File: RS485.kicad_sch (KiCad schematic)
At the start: 11 parts, among them U12 ADM1491EBR

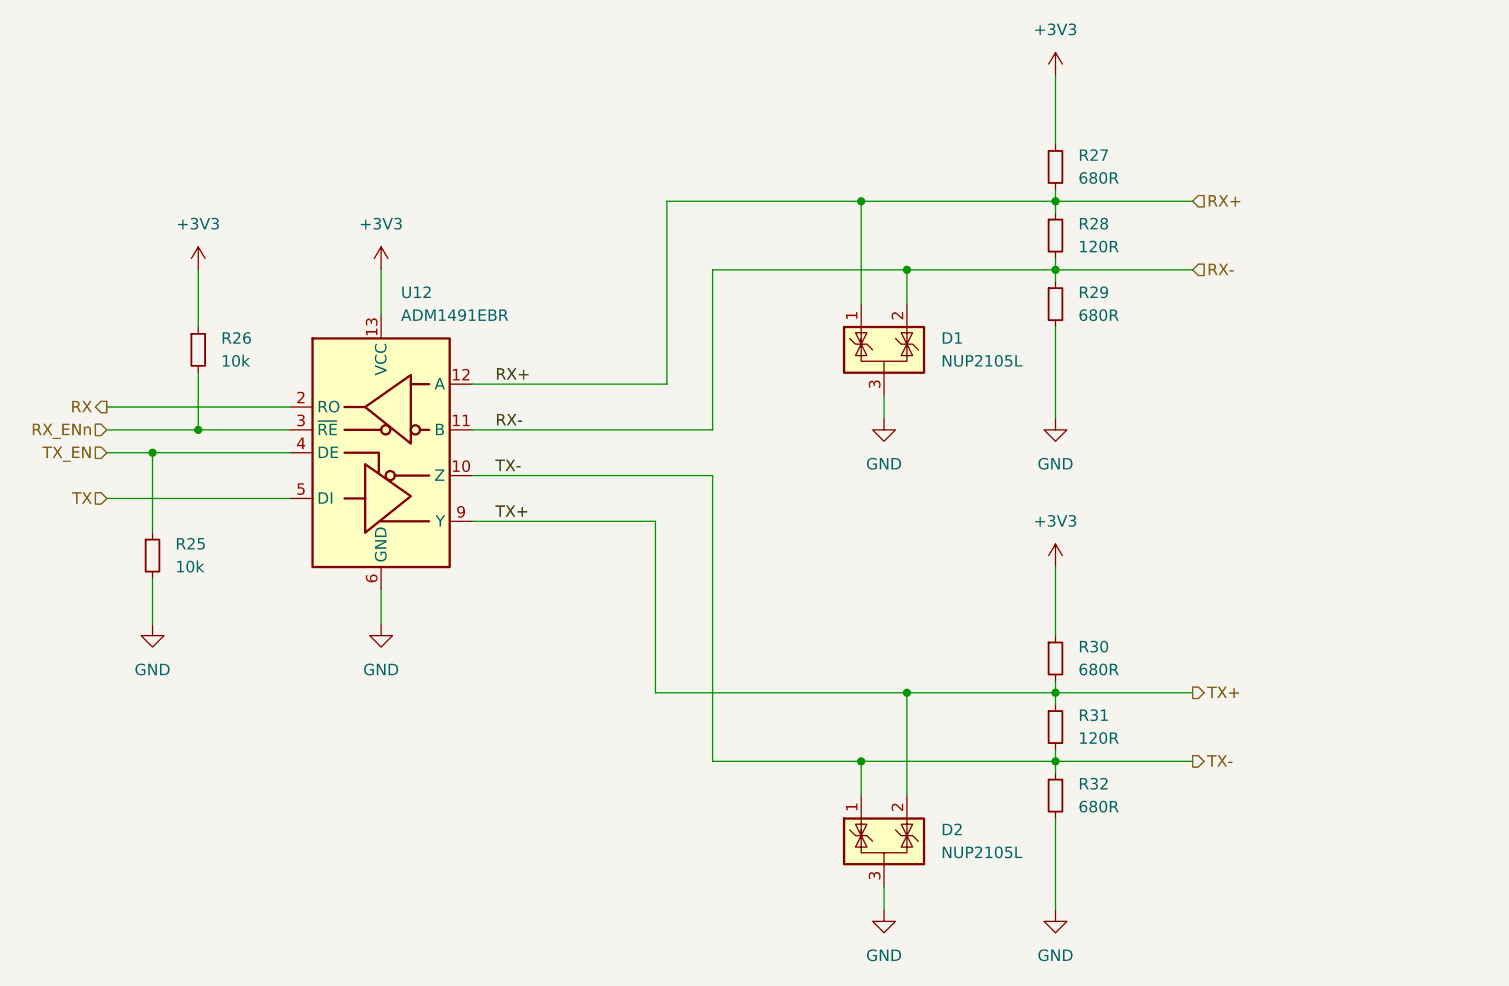
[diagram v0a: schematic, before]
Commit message: Updated i2c device addresses and mcu caps
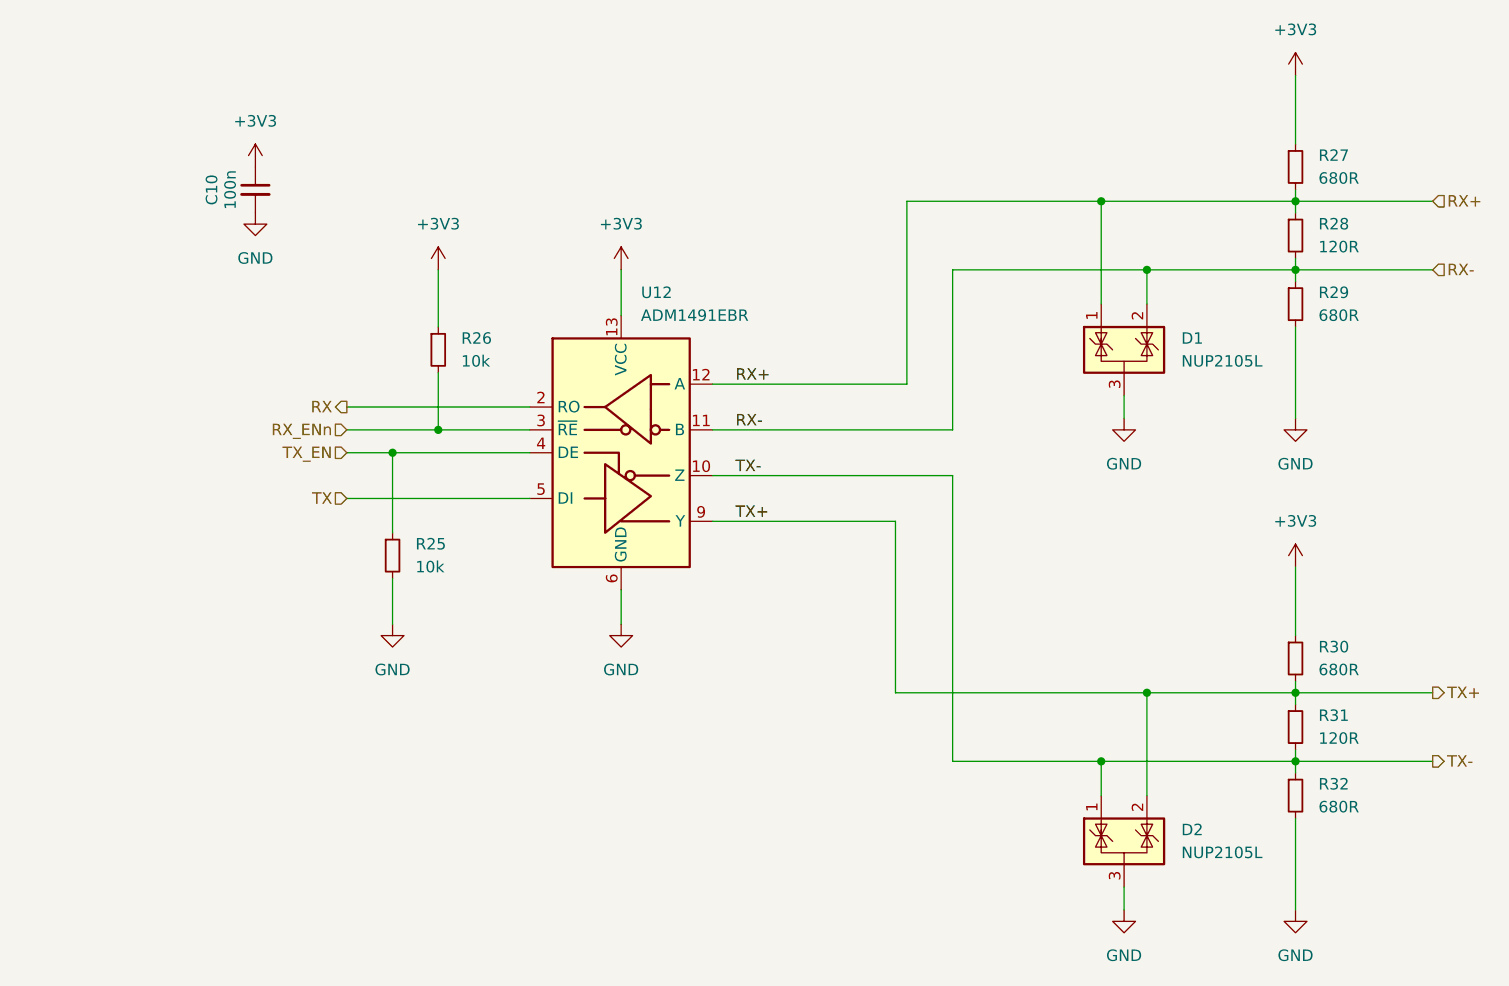
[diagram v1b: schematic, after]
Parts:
- added C10: 100n, Capacitor_SMD:C_0603_1608Metric, symbol Device:C_Small
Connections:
- net +3V3: now also C10.1
- net GND: now also C10.2
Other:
- moved on the sheet: D1, D2, R25, R26, R27, R28, R29, R30, R31, R32, U12

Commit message: Updated version to v2.1
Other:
- company: (none) -> Carnegie Mellon University
- title: (none) -> Argus Mainboard
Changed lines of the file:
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@@
 	(generator_version "8.0")
 	(paper "A4")
+	(title_block
+		(title "Argus Mainboard")
+		(date "2024-11-19")
+		(rev "v2.1")
+		(company "Carnegie Mellon University")
+		(comment 1 "M. Holliday")
+		(comment 2 "N. Khera")
+		(comment 3 "V. Rajesh")
+	)
 	(junction
 		(at 99.06 96.52)
